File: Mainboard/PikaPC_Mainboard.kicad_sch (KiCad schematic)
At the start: 67 parts, among them J10 Conn_01x08, J11 Conn_01x08, J12 Conn_01x08, J13 Conn_01x08, J14 Conn_01x08, J15 Conn_01x08, J16 Conn_01x08, J17 Conn_01x08, J18 Conn_01x10, J19 Conn_02x05_Odd_Even, J5 DIN41612_03x32_C_Split, J9 Conn_01x08, SW1 SW_Push_DPDT, SW2 SW_Push, U1 PPC403GA, U10 74LS07, U101 SN74LVC245A, U102 SN74LVC245A, U103 SN74LVC245A, U104 SN74LVC245A, U105 SN74LVC245A, U106 SN74LVC245A, U107 SN74LVC245A, U108 SN74LVC245A, U109 74LS244, U110 74LS244, U111 74LS244, U112 74LS244, U12 GD75232N, U13 74LVC125, U14 MCP120-315GI/TO, U15 AS6C4008-55PCN, U16 AS6C4008-55PCN, U2 ATF1508AS, U3 SST39VF010, U4 74AHCT244, U9 74LS04, Y1 25M, Y2 7M3728

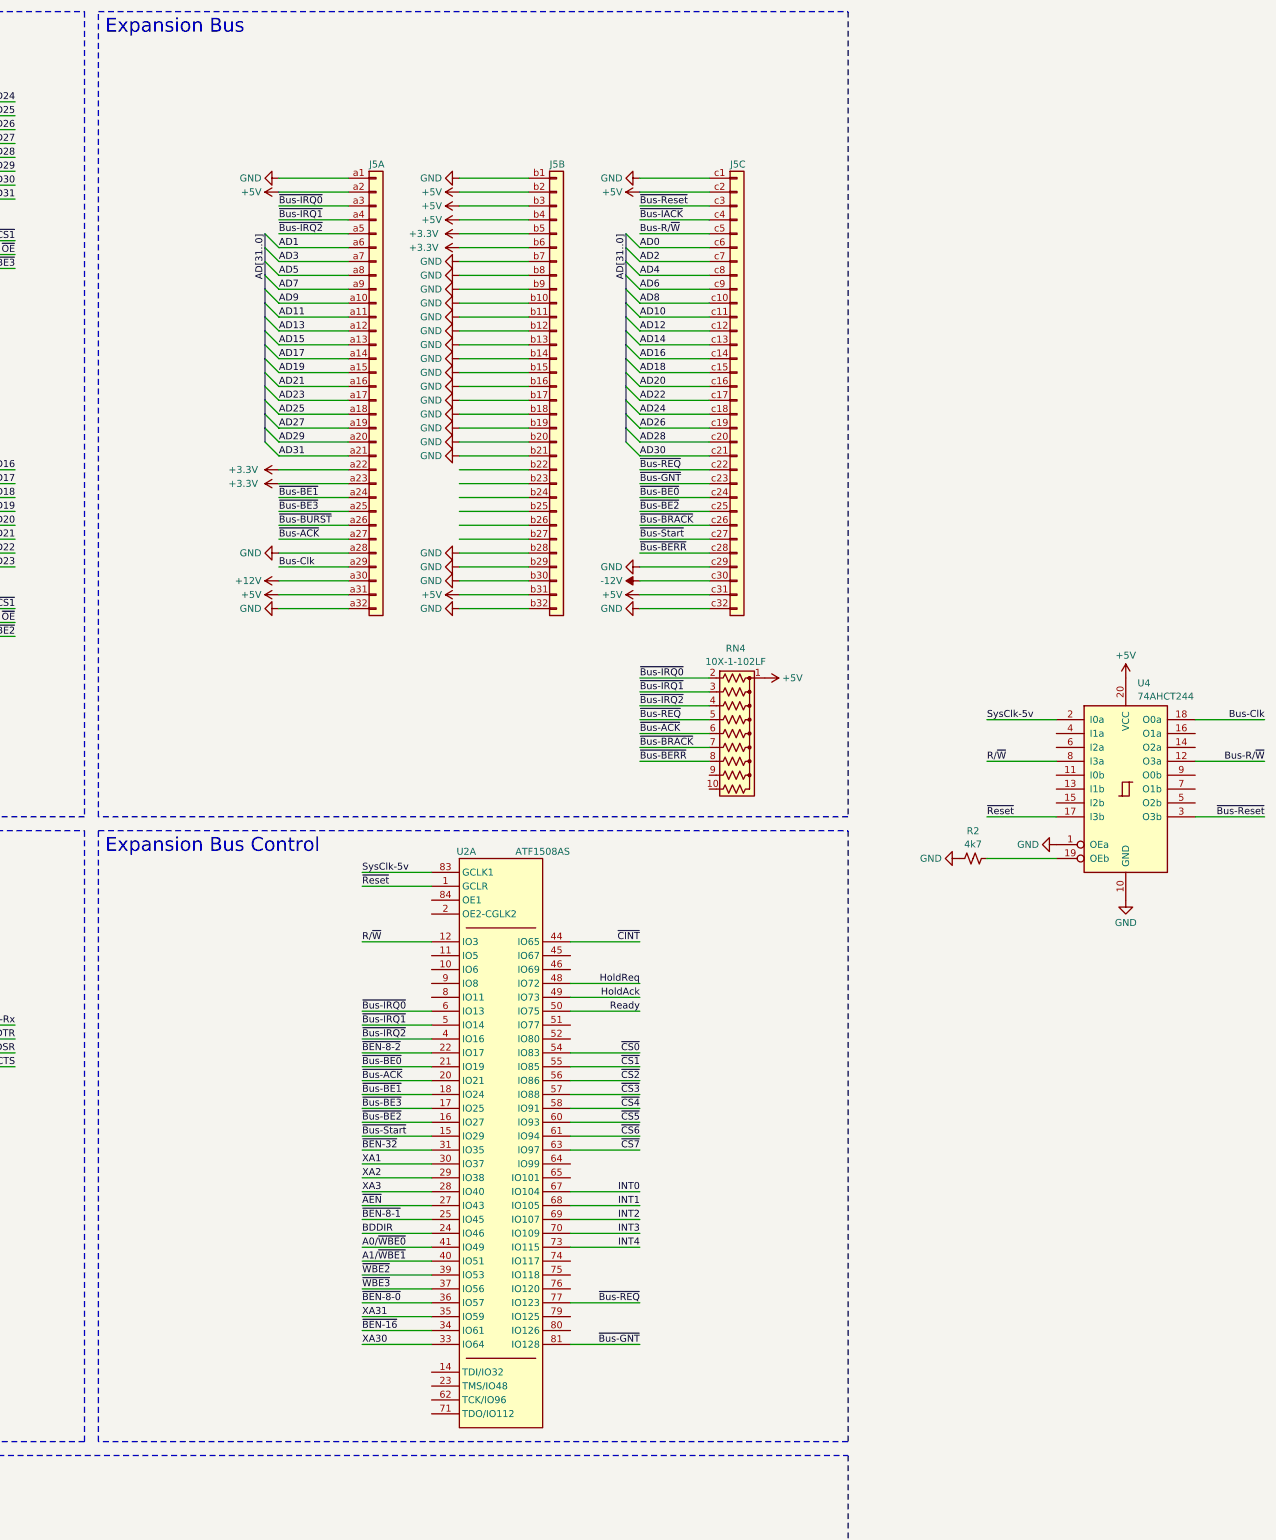
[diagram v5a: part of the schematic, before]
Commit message: add pull-down resistors to AD bus
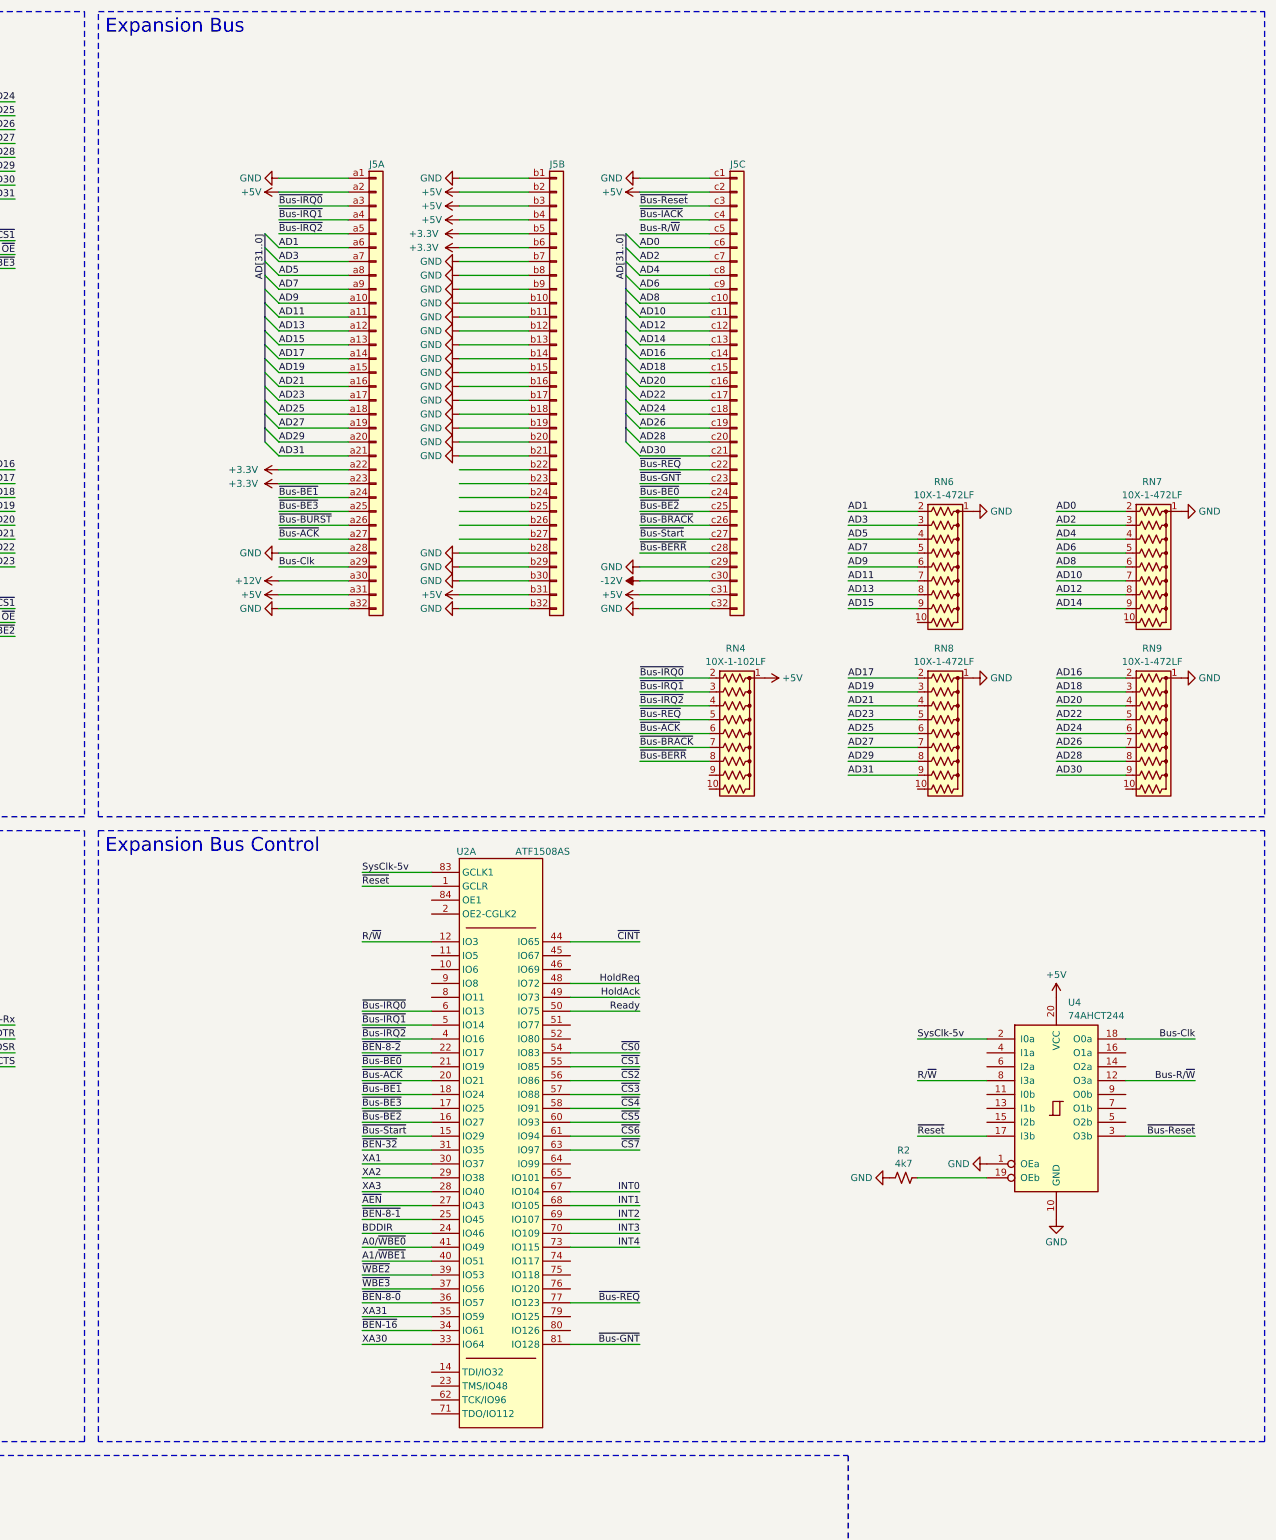
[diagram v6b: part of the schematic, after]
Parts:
- added RN6, RN7, RN8, RN9: 10X-1-472LF, Resistor_THT:R_Array_SIP10, symbol Device:R_Network09_US
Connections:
- net AD0: now also RN7.2 (R1)
- net AD1: now also RN6.2 (R1)
- net AD10: now also RN7.7 (R6)
- net AD11: now also RN6.7 (R6)
- net AD12: now also RN7.8 (R7)
- net AD13: now also RN6.8 (R7)
- net AD14: now also RN7.9 (R8)
- net AD15: now also RN6.9 (R8)
- net AD16: now also RN9.2 (R1)
- net AD17: now also RN8.2 (R1)
- net AD18: now also RN9.3 (R2)
- net AD19: now also RN8.3 (R2)
- net AD2: now also RN7.3 (R2)
- net AD20: now also RN9.4 (R3)
- net AD21: now also RN8.4 (R3)
- net AD22: now also RN9.5 (R4)
- net AD23: now also RN8.5 (R4)
- net AD24: now also RN9.6 (R5)
- net AD25: now also RN8.6 (R5)
- net AD26: now also RN9.7 (R6)
- net AD27: now also RN8.7 (R6)
- net AD28: now also RN9.8 (R7)
- net AD29: now also RN8.8 (R7)
- net AD3: now also RN6.3 (R2)
- net AD30: now also RN9.9 (R8)
- net AD31: now also RN8.9 (R8)
- net AD4: now also RN7.4 (R3)
- net AD5: now also RN6.4 (R3)
- net AD6: now also RN7.5 (R4)
- net AD7: now also RN6.5 (R4)
- net AD8: now also RN7.6 (R5)
- net AD9: now also RN6.6 (R5)
- net GND: now also RN6.1 (common), RN7.1 (common), RN8.1 (common), RN9.1 (common)
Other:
- moved on the sheet: R2, U4

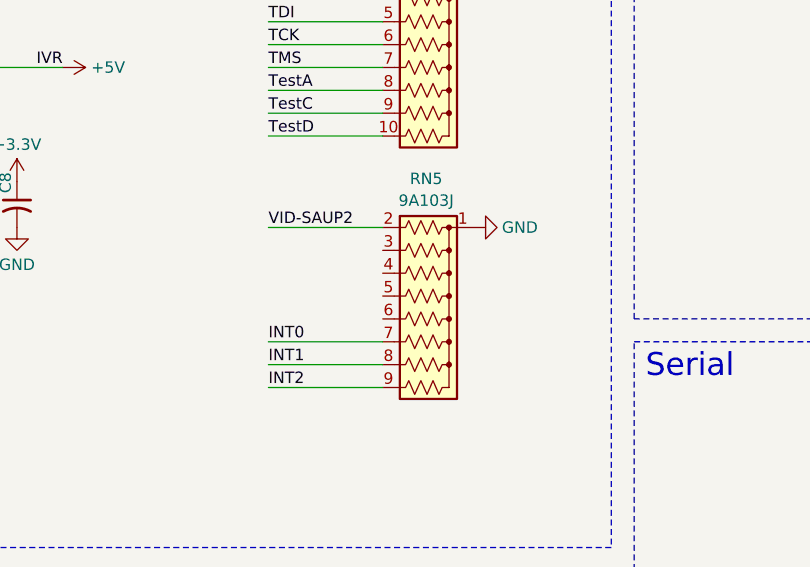
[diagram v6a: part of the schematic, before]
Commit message: Remove redundant SIP resistor from mainboard
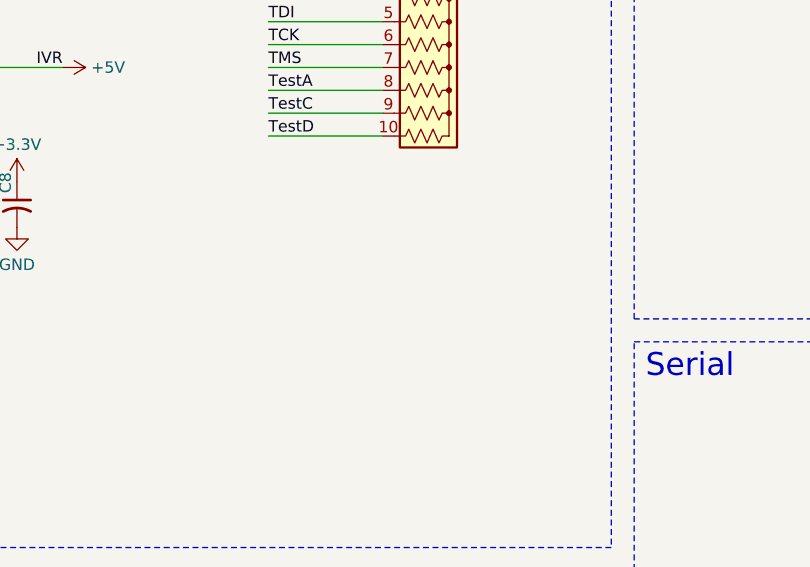
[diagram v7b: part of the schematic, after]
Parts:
- removed RN5: 9A103J, Resistor_THT:R_Array_SIP9, symbol Device:R_Network08_US
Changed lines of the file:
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@@
 	(wire
 		(pts
-			(xy 228.6 172.72) (xy 241.3 172.72)
-		)
-		(stroke
-			(width 0)
-			(type default)
-		)
-	)
-	(wire
-		(pts
 			(xy 330.2 393.7) (xy 317.5 393.7)
 		)
@@
 	(wire
 		(pts
-			(xy 228.6 170.18) (xy 241.3 170.18)
-		)
-		(stroke
-			(width 0)
-			(type default)
-		)
-	)
-	(wire
-		(pts
 			(xy 165.1 335.28) (xy 152.4 335.28)
 		)
@@
 	(wire
 		(pts
-			(xy 228.6 167.64) (xy 241.3 167.64)
-		)
-		(stroke
-			(width 0)
-			(type default)
-		)
-	)
-	(wire
-		(pts
 			(xy 474.98 73.66) (xy 487.68 73.66)
 		)
@@
 	(wire
 		(pts
-			(xy 228.6 154.94) (xy 241.3 154.94)
-		)
-		(stroke
-			(width 0)
-			(type default)
-		)
-	)
-	(wire
-		(pts
 			(xy 355.6 340.36) (xy 342.9 340.36)
 		)
@@
 		)
 	)
-	(label "INT0"
-		(at 228.6 167.64 0)
-		(effects
-			(font
-				(size 1.27 1.27)
-			)
-			(justify left bottom)
-		)
-	)
 	(label "AD8"
 		(at 457.2 381 180)
@@
 		)
 	)
-	(label "VID-SAUP2"
-		(at 228.6 154.94 0)
-		(effects
-			(font
-				(size 1.27 1.27)
-			)
-			(justify left bottom)
-		)
-	)
 	(label "D30"
 		(at 152.4 327.66 0)
@@
 		)
 	)
-	(label "INT1"
-		(at 228.6 170.18 0)
-		(effects
-			(font
-				(size 1.27 1.27)
-			)
-			(justify left bottom)
-		)
-	)
 	(label "AD13"
 		(at 266.7 330.2 180)
@@
 		)
 	)
-	(label "INT2"
-		(at 228.6 172.72 0)
-		(effects
-			(font
-				(size 1.27 1.27)
-			)
-			(justify left bottom)
-		)
-	)
 	(label "A7"
 		(at 276.86 52.07 0)
@@
 	)
 	(symbol
-		(lib_id "Device:R_Network08_US")
-		(at 246.38 165.1 270)
-		(unit 1)
-		(exclude_from_sim no)
-		(in_bom yes)
-		(on_board yes)
-		(dnp no)
-		(fields_autoplaced yes)
-		(property "Reference" "RN5"
-			(at 246.126 149.5255 90)
-			(effects
-				(font
-					(size 1.27 1.27)
-				)
-			)
-		)
-		(property "Value" "9A103J"
-			(at 246.126 151.9498 90)
-			(effects
-				(font
-					(size 1.27 1.27)
-				)
-			)
-		)
-		(property "Footprint" "Resistor_THT:R_Array_SIP9"
-			(at 246.38 177.165 90)
-			(effects
-				(font
-					(size 1.27 1.27)
-				)
-				(hide yes)
-			)
-		)
-		(property "Datasheet" "http://www.vishay.com/docs/31509/csc.pdf"
-			(at 246.38 165.1 0)
-			(effects
-				(font
-					(size 1.27 1.27)
-				)
-				(hide yes)
-			)
-		)
-		(property "Description" "8 resistor network, star topology, bussed resistors, small US symbol"
-			(at 246.38 165.1 0)
-			(effects
-				(font
-					(size 1.27 1.27)
-				)
-				(hide yes)
-			)
-		)
-		(pin "5"
-		)
-		(pin "8"
-		)
-		(pin "7"
-		)
-		(pin "3"
-		)
-		(pin "1"
-		)
-		(pin "4"
-		)
-		(pin "6"
-		)
-		(pin "2"
-		)
-		(pin "9"
-		)
-		(instances
-			(project "PikaPC_Mainboard"
-				(path "/31647a00-1631-4687-a4ca-8a073377aae5"
-					(reference "RN5")
-					(unit 1)
-				)
-			)
-		)
-	)
-	(symbol
 		(lib_id "74xx:74LS245")
 		(at 177.8 393.7 0)
@@
 					(unit 1)
 				)
-			)
-		)
-	)
-	(symbol
-		(lib_id "power:GND")
-		(at 251.46 154.94 90)
-		(unit 1)
-		(exclude_from_sim no)
-		(in_bom yes)
-		(on_board yes)
-		(dnp no)
-		(property "Reference" "#PWR034"
-			(at 257.81 154.94 0)
-			(effects
-				(font
-					(size 1.27 1.27)
-				)
-				(hide yes)
-			)
-		)
-		(property "Value" "GND"
-			(at 256.54 154.94 90)
-			(effects
-				(font
-					(size 1.27 1.27)
-				)
-			)
-		)
-		(property "Footprint" ""
-			(at 251.46 154.94 0)
-			(effects
-				(font
-					(size 1.27 1.27)
-				)
-				(hide yes)
-			)
-		)
-		(property "Datasheet" ""
-			(at 251.46 154.94 0)
-			(effects
-				(font
-					(size 1.27 1.27)
-				)
-				(hide yes)
-			)
-		)
-		(property "Description" "Power symbol creates a global label with name \"GND\" , ground"
-			(at 251.46 154.94 0)
-			(effects
-				(font
-					(size 1.27 1.27)
-				)
-				(hide yes)
-			)
-		)
-		(pin "1"
-		)
-		(instances
-			(project "PikaPC_Mainboard"
-				(path "/31647a00-1631-4687-a4ca-8a073377aae5"
-					(reference "#PWR034")
-					(unit 1)
-				)
